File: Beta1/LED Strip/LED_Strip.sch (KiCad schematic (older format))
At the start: 100 parts, among them U0 APA102C, U1 APA102C, U10 APA102C, U11 APA102C, U12 APA102C, U13 APA102C, U14 APA102C, U15 APA102C, U2 APA102C, U3 APA102C, U4 APA102C, U5 APA102C, U6 APA102C, U7 APA102C, U8 APA102C, U9 APA102C

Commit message: Placed all LED components
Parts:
- added C16, C17, C18, C19, C20, C21, C22, C23, C24, C25, C26, C27, C28, C29, C30, C31: 0.1u, Capacitors_SMD:C_0603, symbol C
- added CLK16, CLKOUT31, D16, DOUT31: CONN_01X01, Liberry:single_0.1, symbol CONN_01X01
- added CLK17, CLK18, CLK19, CLK20, CLK21, CLK22, CLK23, CLK24, CLK25, CLK26, CLK27, CLK28, CLK29, CLK30, CLK31, CLK32, D17, D18, D19, D20, D21, D22, D23, D24, D25, D26, D27, D28, D29, D30, D31, D32: CONN_01X01, Liberry:TESTPAD, symbol CONN_01X01
- added RC16, RC17, RC18, RC19, RC20, RC21, RC22, RC23, RC24, RC25, RC26, RC27, RC28, RC29, RC30, RC31, RD16, RD17, RD18, RD19, RD20, RD21, RD22, RD23, RD24, RD25, RD26, RD27, RD28, RD29, RD30, RD31: ZERO, Resistors_SMD:R_0603, symbol R
- added U16, U17, U18, U19, U20, U21, U22, U23, U24, U25, U26, U27, U28, U29, U30, U31: APA102C, Liberry:PLCC6-1.6x4.2_LED, symbol APA102C
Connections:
- net labels added: CLK24, CLK32, D24, D32
- wire segments 266 -> 530
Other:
- moved on the sheet: C0, C1, C10, C11, C12, C13, C14, C15, C2, C3, C4, C5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

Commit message: Placed all LED strip components. Only routing remains
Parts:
- removed CLKOUT1, DOUT1: CONN_01X01, Liberry:single_0.1, symbol CONN_01X01
- added +3.3V_IN1, CS_LED1, GND2, MOSI1, SPI_CLK1: CONN_01X01, Liberry:single_0.1, symbol CONN_01X01
- added C32, C33, C34: 0.1u, Capacitors_SMD:C_0603, symbol C
- added U32: SN74LV1T125DBVR, Liberry:SOT23-5, symbol SN74LV1T125DBVR
- added U33: SN74LVC2T45DCTT, Liberry:SSOP8, symbol SN74LVC2T45DCTT
- renumbered VCC0 to +5V_IN1
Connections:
- net +5V: now also C34.1, U33.8 (VCCB)
- net GND: now also C32.2, C33.2, C34.2, GND2.1 (P1), U32.3 (GND), U33.4 (GND), U33.5 (DIR)
- net at CLK0.1 (P1), RC0.1, U0.2 (CI): now also U33.6 (B2)
- net at D0.1 (P1), RD0.1, U0.1 (DI): now also U33.7 (B1)
- new net: CS_LED1.1 (P1), U32.1 (!OE)
- new net: SPI_CLK1.1 (P1), U32.2 (A)
- new net: U32.4 (Y), U33.3 (A2)
- new net: MOSI1.1 (P1), U33.2 (A1)
- new net +3V3: +3.3V_IN1.1 (P1), C32.1, C33.1, U32.5 (VCC), U33.1 (VCCA)

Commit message: Converted vias to plated through holes. Vias are / can be tented over.
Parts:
- added +3.3V_INB1, +5V_INB1, CLKB0, CLKB16, CLKOUTB31, CS_LEDB1, DB0, DB16, DOUTB31, GNDB0, GNDB2, MOSIB1, SPI_CLKB1: CONN_01X01, Liberry:single_0.1, symbol CONN_01X01
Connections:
- net +3V3: now also +3.3V_INB1.1 (P1)
- net +5V: now also +5V_INB1.1 (P1)
- net CLK16: now also CLKB16.1 (P1)
- net CLK32: now also CLKOUTB31.1 (P1)
- net D16: now also DB16.1 (P1)
- net D32: now also DOUTB31.1 (P1)
- net GND: now also GNDB0.1 (P1), GNDB2.1 (P1)
- net at CLK0.1 (P1), RC0.1, U0.2 (CI)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: now also CLKB0.1 (P1)
- net at D0.1 (P1), RD0.1, U0.1 (DI)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: now also DB0.1 (P1)
- net at CS_LED1.1 (P1), U32.1 (!OE): now also CS_LEDB1.1 (P1)
- net at SPI_CLK1.1 (P1), U32.2 (A): now also SPI_CLKB1.1 (P1)
- net at MOSI1.1 (P1), U33.2 (A1): now also MOSIB1.1 (P1)
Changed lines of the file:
@@
 U 1 1 582CB028
 P 9400 1600
-F 0 "+5V_IN1" H 9550 1600 50  0000 C CNN
+F 0 "+5V_IN1" H 9650 1600 50  0000 C CNN
 F 1 "CONN_01X01" V 9500 1600 50  0001 C CNN
 F 2 "Liberry:single_0.1" H 9400 1600 50  0001 C CNN
@@
 U 1 1 582CB040
 P 9400 2000
-F 0 "GND0" H 9550 2000 50  0000 C CNN
+F 0 "GND0" H 9600 2000 50  0000 C CNN
 F 1 "CONN_01X01" V 9500 2000 50  0001 C CNN
 F 2 "Liberry:single_0.1" H 9400 2000 50  0001 C CNN
@@
 U 1 1 582E4527
 P 9250 6450
-F 0 "CLK16" H 9400 6450 50  0000 C CNN
+F 0 "CLK16" H 9450 6450 50  0000 C CNN
 F 1 "CONN_01X01" V 9350 6450 50  0001 C CNN
 F 2 "Liberry:single_0.1" H 9250 6450 50  0001 C CNN
@@
 U 1 1 582E455F
 P 28150 9050
-F 0 "DOUT31" H 28300 9050 50  0000 C CNN
+F 0 "DOUT31" H 28400 9050 50  0000 C CNN
 F 1 "CONN_01X01" V 28250 9050 50  0001 C CNN
 F 2 "Liberry:single_0.1" H 28150 9050 50  0001 C CNN
@@
 U 1 1 582E4567
 P 28150 9250
-F 0 "CLKOUT31" H 28300 9250 50  0000 C CNN
+F 0 "CLKOUT31" H 28450 9250 50  0000 C CNN
 F 1 "CONN_01X01" V 28250 9250 50  0001 C CNN
 F 2 "Liberry:single_0.1" H 28150 9250 50  0001 C CNN
@@
 U 1 1 582F5B39
 P 3900 1250
-F 0 "GND2" H 4050 1250 50  0000 C CNN
+F 0 "GND2" H 4100 1250 50  0000 C CNN
 F 1 "CONN_01X01" V 4000 1250 50  0001 C CNN
 F 2 "Liberry:single_0.1" H 3900 1250 50  0001 C CNN
@@
 U 1 1 582F82B7
 P 3800 3250
-F 0 "CS_LED1" H 4150 3250 50  0000 R CNN
+F 0 "CS_LED1" H 4200 3250 50  0000 R CNN
 F 1 "CONN_01X01" V 3900 3250 50  0001 C CNN
 F 2 "Liberry:single_0.1" H 3800 3250 50  0001 C CNN
@@
 U 1 1 582FA47D
 P 3800 3450
-F 0 "SPI_CLK1" H 4150 3450 50  0000 R CNN
+F 0 "SPI_CLK1" H 4250 3450 50  0000 R CNN
 F 1 "CONN_01X01" V 3900 3450 50  0001 C CNN
 F 2 "Liberry:single_0.1" H 3800 3450 50  0001 C CNN
@@
 	9750 1550 9750 2050
 Wire Wire Line
-	9600 1550 9600 1600
+	9600 1550 9600 1700
 Wire Wire Line
 	9600 1250 9600 1350
@@
 	4100 1250 4250 1250
 Wire Wire Line
-	4250 1250 4250 1300
+	4250 1100 4250 1300
 Wire Wire Line
 	5700 3000 5700 2950
@@
 Wire Wire Line
 	7700 2100 7600 2100
+$Comp
+L CONN_01X01 +3.3V_INB1
+U 1 1 582FA675
+P 3900 800
+F 0 "+3.3V_INB1" H 4200 800 50  0000 C CNN
+F 1 "CONN_01X01" V 4000 800 50  0001 C CNN
+F 2 "Liberry:single_0.1" H 3900 800 50  0001 C CNN
+F 3 "" H 3900 800 50  0000 C CNN
+F 4 "PCB" H 3900 800 60  0001 C CNN "MFG"
+F 5 "ON_PCB" H 3900 800 60  0001 C CNN "MPN"
+	1    3900 800
+	-1   0    0    1
+$EndComp
+Wire Wire Line
+	4100 800  4200 800
+Connection ~ 4200 800
+$Comp
+L CONN_01X01 GNDB2
+U 1 1 582FB036
+P 3900 1100
+F 0 "GNDB2" H 4100 1100 50  0000 C CNN
+F 1 "CONN_01X01" V 4000 1100 50  0001 C CNN
+F 2 "Liberry:single_0.1" H 3900 1100 50  0001 C CNN
+F 3 "" H 3900 1100 50  0000 C CNN
+F 4 "PCB" H 3900 1100 60  0001 C CNN "MFG"
+F 5 "ON_PCB" H 3900 1100 60  0001 C CNN "MPN"
+	1    3900 1100
+	-1   0    0    1
+$EndComp
+Wire Wire Line
+	4100 1100 4250 1100
+Connection ~ 4250 1250
+$Comp
+L CONN_01X01 MOSIB1
+U 1 1 582FC7D6
+P 3850 1650
+F 0 "MOSIB1" H 4200 1650 50  0000 R CNN
+F 1 "CONN_01X01" V 3950 1650 50  0001 C CNN
+F 2 "Liberry:single_0.1" H 3850 1650 50  0001 C CNN
+F 3 "" H 3850 1650 50  0000 C CNN
+F 4 "PCB" H 3850 1650 60  0001 C CNN "MFG"
+F 5 "ON_PCB" H 3850 1650 60  0001 C CNN "MPN"
+	1    3850 1650
+	-1   0    0    1
+$EndComp
+Wire Wire Line
+	4050 1650 4100 1650
+Wire Wire Line
+	4100 1650 4100 1800
+Connection ~ 4100 1800
+$Comp
+L CONN_01X01 CS_LEDB1
+U 1 1 582FFB94
+P 3800 3100
+F 0 "CS_LEDB1" H 4250 3100 50  0000 R CNN
+F 1 "CONN_01X01" V 3900 3100 50  0001 C CNN
+F 2 "Liberry:single_0.1" H 3800 3100 50  0001 C CNN
+F 3 "" H 3800 3100 50  0000 C CNN
+F 4 "PCB" H 3800 3100 60  0001 C CNN "MFG"
+F 5 "ON_PCB" H 3800 3100 60  0001 C CNN "MPN"
+	1    3800 3100
+	-1   0    0    1
+$EndComp
+Wire Wire Line
+	4000 3100 4100 3100
+Wire Wire Line
+	4100 3100 4100 3250
+Connection ~ 4100 3250
+$Comp
+L CONN_01X01 SPI_CLKB1
+U 1 1 58300552
+P 3800 3600
+F 0 "SPI_CLKB1" H 4250 3600 50  0000 R CNN
+F 1 "CONN_01X01" V 3900 3600 50  0001 C CNN
+F 2 "Liberry:single_0.1" H 3800 3600 50  0001 C CNN
+F 3 "" H 3800 3600 50  0000 C CNN
+F 4 "PCB" H 3800 3600 60  0001 C CNN "MFG"
+F 5 "ON_PCB" H 3800 3600 60  0001 C CNN "MPN"
+	1    3800 3600
+	-1   0    0    1
+$EndComp
+Wire Wire Line
+	4000 3600 4100 3600
+Wire Wire Line
+	4100 3600 4100 3450
+Connection ~ 4100 3450
+$Comp
+L CONN_01X01 +5V_INB1
+U 1 1 5830473A
+P 9400 1700
+F 0 "+5V_INB1" H 9650 1700 50  0000 C CNN
+F 1 "CONN_01X01" V 9500 1700 50  0001 C CNN
+F 2 "Liberry:single_0.1" H 9400 1700 50  0001 C CNN
+F 3 "" H 9400 1700 50  0000 C CNN
+F 4 "PCB" H 9400 1700 60  0001 C CNN "MFG"
+F 5 "ON_PCB" H 9400 1700 60  0001 C CNN "MPN"
+	1    9400 1700
+	-1   0    0    1
+$EndComp
+Connection ~ 9600 1600
+$Comp
+L CONN_01X01 GNDB0
+U 1 1 58305CC4
+P 9400 1900
+F 0 "GNDB0" H 9600 1900 50  0000 C CNN
+F 1 "CONN_01X01" V 9500 1900 50  0001 C CNN
+F 2 "Liberry:single_0.1" H 9400 1900 50  0001 C CNN
+F 3 "" H 9400 1900 50  0000 C CNN
+F 4 "PCB" H 9400 1900 60  0001 C CNN "MFG"
+F 5 "ON_PCB" H 9400 1900 60  0001 C CNN "MPN"
+	1    9400 1900
+	-1   0    0    1
+$EndComp
+Wire Wire Line
+	9600 1900 9750 1900
+Connection ~ 9750 1900
+$Comp
+L CONN_01X01 CLKB0
+U 1 1 583096B9
+P 8850 1250
+F 0 "CLKB0" H 9050 1250 50  0000 C CNN
+F 1 "CONN_01X01" V 8950 1250 50  0001 C CNN
+F 2 "Liberry:single_0.1" H 8850 1250 50  0001 C CNN
+F 3 "" H 8850 1250 50  0000 C CNN
+F 4 "PCB" H 8850 1250 60  0001 C CNN "MFG"
+F 5 "ON_PCB" H 8850 1250 60  0001 C CNN "MPN"
+	1    8850 1250
+	-1   0    0    1
+$EndComp
+Wire Wire Line
+	9050 1250 9050 1350
+Connection ~ 9050 1350
+$Comp
+L CONN_01X01 DB0
+U 1 1 5830A4E1
+P 8850 1050
+F 0 "DB0" H 9000 1050 50  0000 C CNN
+F 1 "CONN_01X01" V 8950 1050 50  0001 C CNN
+F 2 "Liberry:single_0.1" H 8850 1050 50  0001 C CNN
+F 3 "" H 8850 1050 50  0000 C CNN
+F 4 "PCB" H 8850 1050 60  0001 C CNN "MFG"
+F 5 "ON_PCB" H 8850 1050 60  0001 C CNN "MPN"
+	1    8850 1050
+	-1   0    0    1
+$EndComp
+Wire Wire Line
+	9050 1050 9050 1150
+Connection ~ 9050 1150
+$Comp
+L CONN_01X01 DOUTB31
+U 1 1 58311E0F
+P 28150 8900
+F 0 "DOUTB31" H 28400 8900 50  0000 C CNN
+F 1 "CONN_01X01" V 28250 8900 50  0001 C CNN
+F 2 "Liberry:single_0.1" H 28150 8900 50  0001 C CNN
+F 3 "" H 28150 8900 50  0000 C CNN
+F 4 "PCB" H 28150 8900 60  0001 C CNN "MFG"
+F 5 "ON_PCB" H 28150 8900 60  0001 C CNN "MPN"
+	1    28150 8900
+	1    0    0    -1
+$EndComp
+Wire Wire Line
+	27950 8900 27900 8900
+Wire Wire Line
+	27900 8900 27900 9050
+Connection ~ 27900 9050
+$Comp
+L CONN_01X01 CLKOUTB31
+U 1 1 58312577
+P 28150 9400
+F 0 "CLKOUTB31" H 28450 9400 50  0000 C CNN
+F 1 "CONN_01X01" V 28250 9400 50  0001 C CNN
+F 2 "Liberry:single_0.1" H 28150 9400 50  0001 C CNN
+F 3 "" H 28150 9400 50  0000 C CNN
+F 4 "PCB" H 28150 9400 60  0001 C CNN "MFG"
+F 5 "ON_PCB" H 28150 9400 60  0001 C CNN "MPN"
+	1    28150 9400
+	1    0    0    -1
+$EndComp
+Wire Wire Line
+	27950 9400 27900 9400
+Wire Wire Line
+	27900 9400 27900 9250
+Connection ~ 27900 9250
+$Comp
+L CONN_01X01 DB16
+U 1 1 5832C873
+P 8700 6200
+F 0 "DB16" H 8850 6200 50  0000 C CNN
+F 1 "CONN_01X01" V 8800 6200 50  0001 C CNN
+F 2 "Liberry:single_0.1" H 8700 6200 50  0001 C CNN
+F 3 "" H 8700 6200 50  0000 C CNN
+F 4 "PCB" H 8700 6200 60  0001 C CNN "MFG"
+F 5 "ON_PCB" H 8700 6200 60  0001 C CNN "MPN"
+	1    8700 6200
+	-1   0    0    1
+$EndComp
+$Comp
+L CONN_01X01 CLKB16
+U 1 1 5832CB2F
+P 9250 6700
+F 0 "CLKB16" H 9450 6700 50  0000 C CNN
+F 1 "CONN_01X01" V 9350 6700 50  0001 C CNN
+F 2 "Liberry:single_0.1" H 9250 6700 50  0001 C CNN
+F 3 "" H 9250 6700 50  0000 C CNN
+F 4 "PCB" H 9250 6700 60  0001 C CNN "MFG"
+F 5 "ON_PCB" H 9250 6700 60  0001 C CNN "MPN"
+	1    9250 6700
+	-1   0    0    1
+$EndComp
+Wire Wire Line
+	8900 6200 9000 6200
+Wire Wire Line
+	9000 6200 9000 6350
+Connection ~ 9000 6350
+Wire Wire Line
+	9450 6700 9500 6700
+Wire Wire Line
+	9500 6700 9500 6550
+Connection ~ 9500 6550
 $EndSCHEMATC

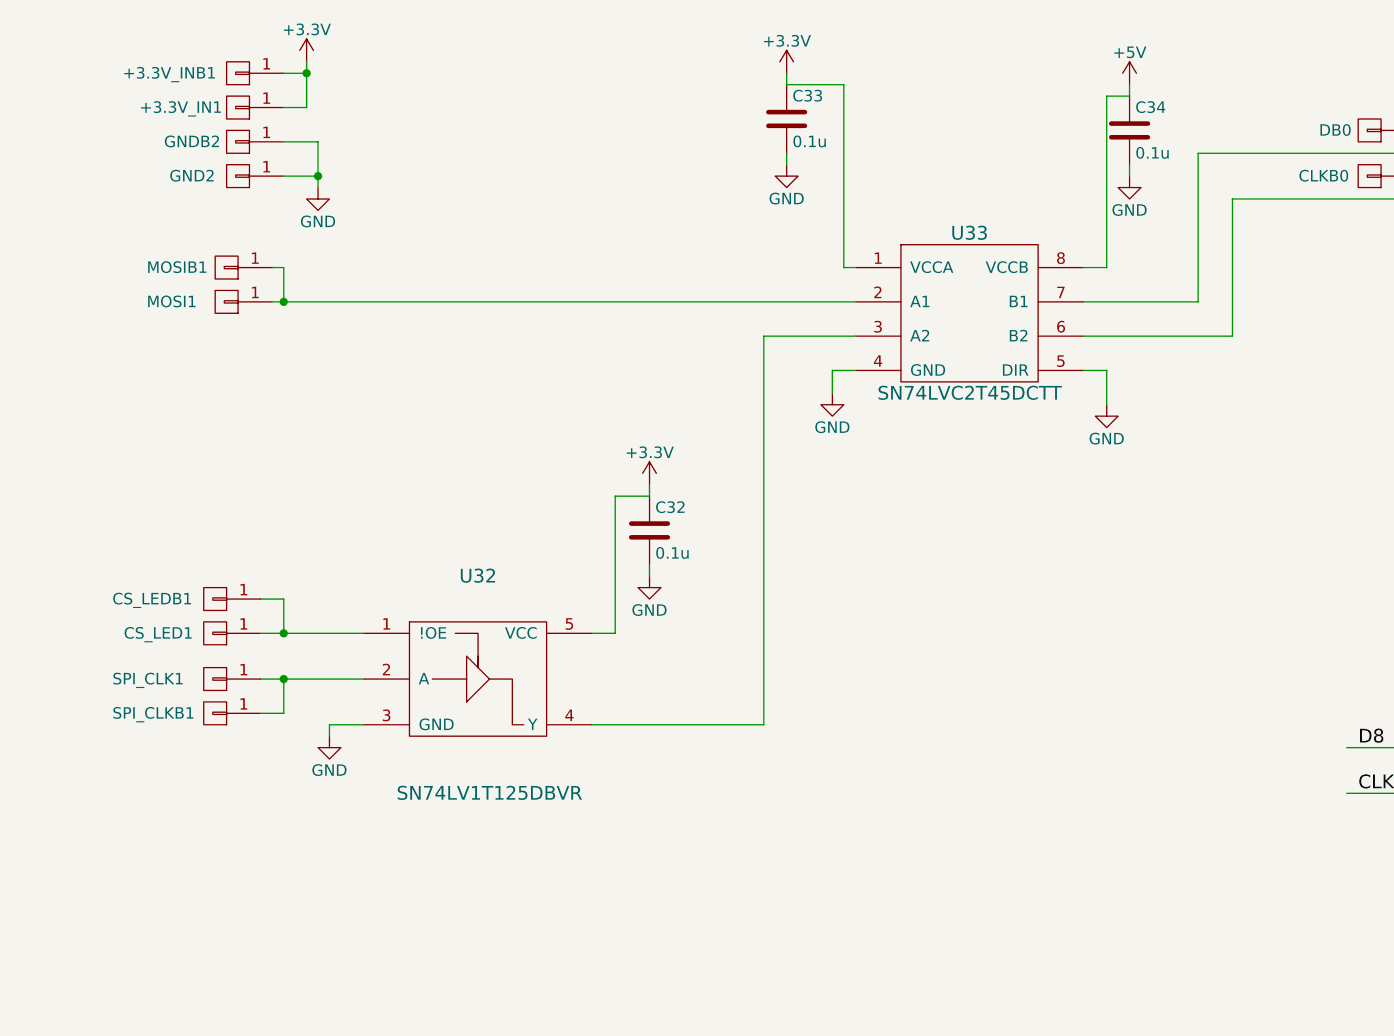
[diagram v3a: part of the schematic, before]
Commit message: Catchup Commit.  Non-atomic, Refactored LED, Keyboard, KeyPAD, and Knobs PCBs
LED: Changed chips. Cleaned up silkscreen text. Added some support
mounting holes. Shrank height of board to avoid stackup. KeyPAD is
updated with new footprint. Keyboard and Knobs are unknown.
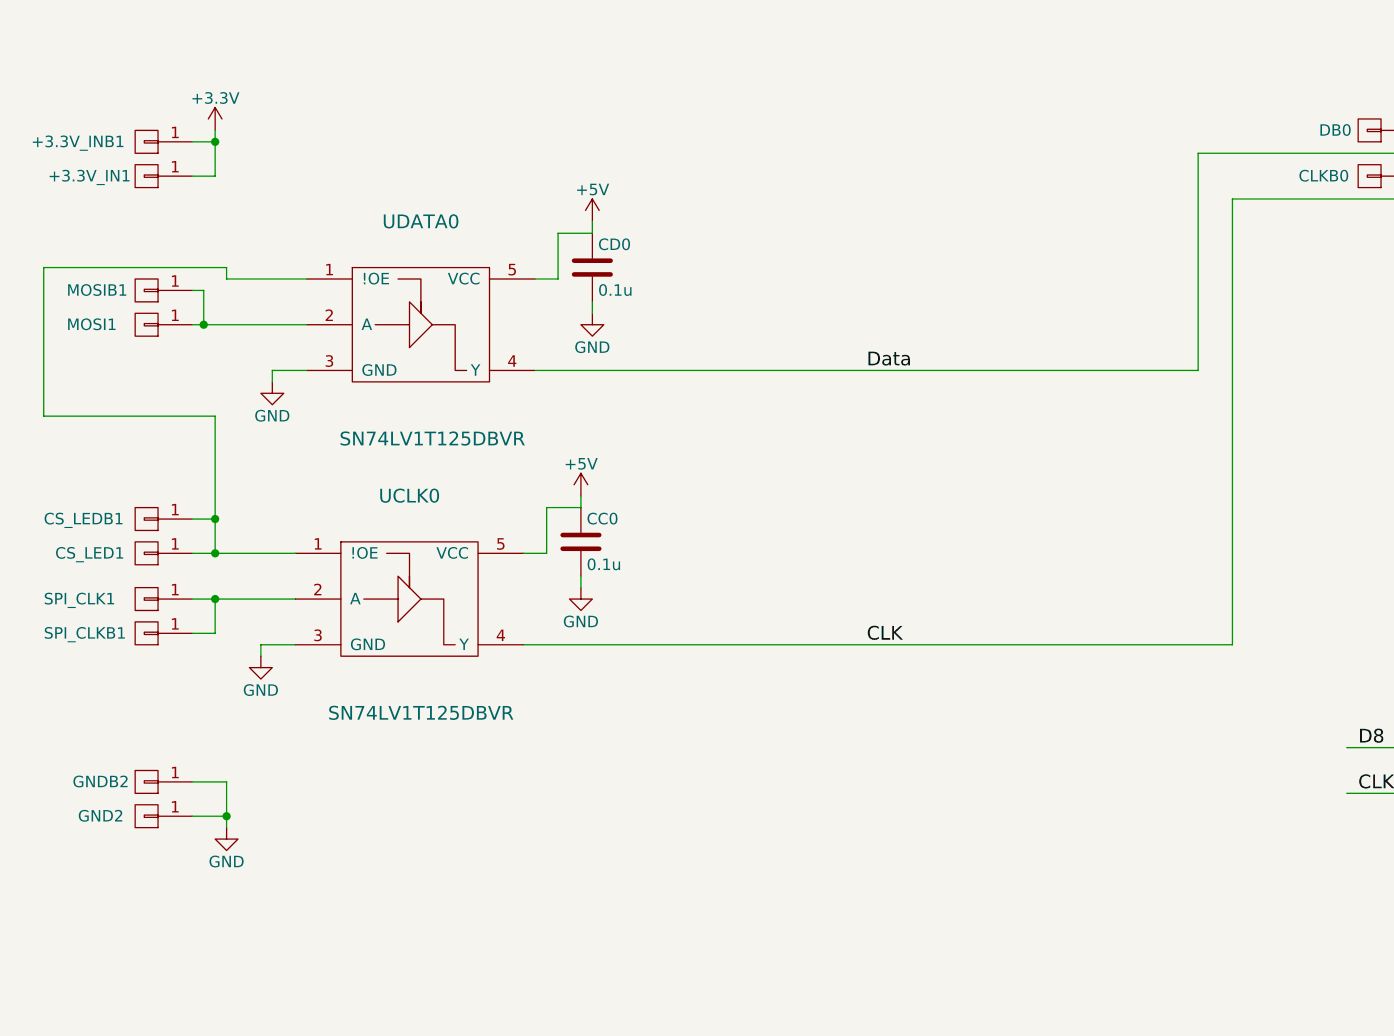
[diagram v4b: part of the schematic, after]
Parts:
- removed C33, C34: 0.1u, Capacitors_SMD:C_0603, symbol C
- removed U33: SN74LVC2T45DCTT, Liberry:SSOP8, symbol SN74LVC2T45DCTT
- added CD0: 0.1u, Capacitors_SMD:C_0603, symbol C
- added UDATA0: SN74LV1T125DBVR, Liberry:SOT23-5, symbol SN74LV1T125DBVR
- renumbered C32 to CC0, U32 to UCLK0
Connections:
- net +3V3: no longer CC0.1, UCLK0.5 (VCC)
- net +5V: now also CC0.1, UCLK0.5 (VCC), CD0.1, UDATA0.5 (VCC)
- net GND: now also CD0.2, UDATA0.3 (GND)
- net CLK: now reaches CLK0.1 (P1), CLKB0.1 (P1), RC0.1, U0.2 (CI)
- net CLK: now also UCLK0.4 (Y)
- net Data: now reaches D0.1 (P1), DB0.1 (P1), RD0.1, U0.1 (DI)
- net Data: now also UDATA0.4 (Y)
- net at CS_LED1.1 (P1), CS_LEDB1.1 (P1), UCLK0.1 (!OE): now also UDATA0.1 (!OE)
- net at MOSI1.1 (P1), MOSIB1.1 (P1): now also UDATA0.2 (A)
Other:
- moved on the sheet: +3.3V_IN1, +3.3V_INB1, CC0, CS_LED1, CS_LEDB1, GND2, GNDB2, MOSI1, MOSIB1, SPI_CLK1, SPI_CLKB1, UCLK0
